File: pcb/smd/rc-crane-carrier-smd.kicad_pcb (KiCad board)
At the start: 2 copper layers, 90 x 64 mm, 32 parts, among them J1 BAT 2-3S, J10 SuperMini L, J11 SuperMini R, J12 DIAG0, J13 DIAG1, J2 Motor lift, J3 Motor tele, J4 RC lift, J5 RC tele, U2 TMC2209 #0 lift, U3 TMC2209 #1 tele, U4 AMS1117-5.0

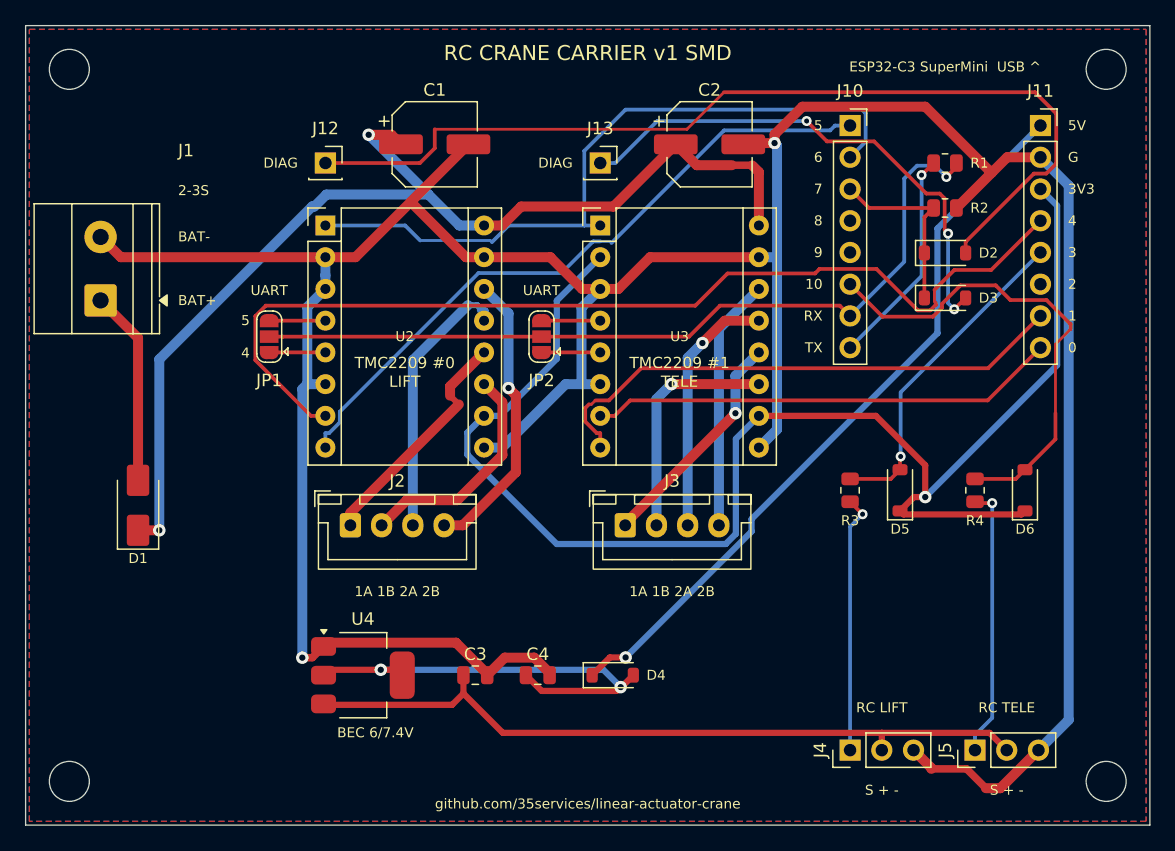
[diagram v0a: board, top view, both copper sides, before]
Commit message: PCB: power the drivers from the BEC, drop the battery input
The drivers' VM now comes from the ESC's BEC (6 V / 7.4 V, 4 A) through
the RC headers, like the ESP32's regulator. Removes the battery
terminal J1 and the reverse polarity diode D1 (the + pin in the middle
of the S + - header makes a reversed servo plug harmless), and the
board shrinks to 80 x 64 mm. Both variants: DRC 0 violations,
0 unconnected.

Co-Authored-By: Claude Opus 5.5 <noreply@anthropic.com>
Claude-Session: https://claude.ai/code/session_01JATcLE25KWRaki615r1Lis
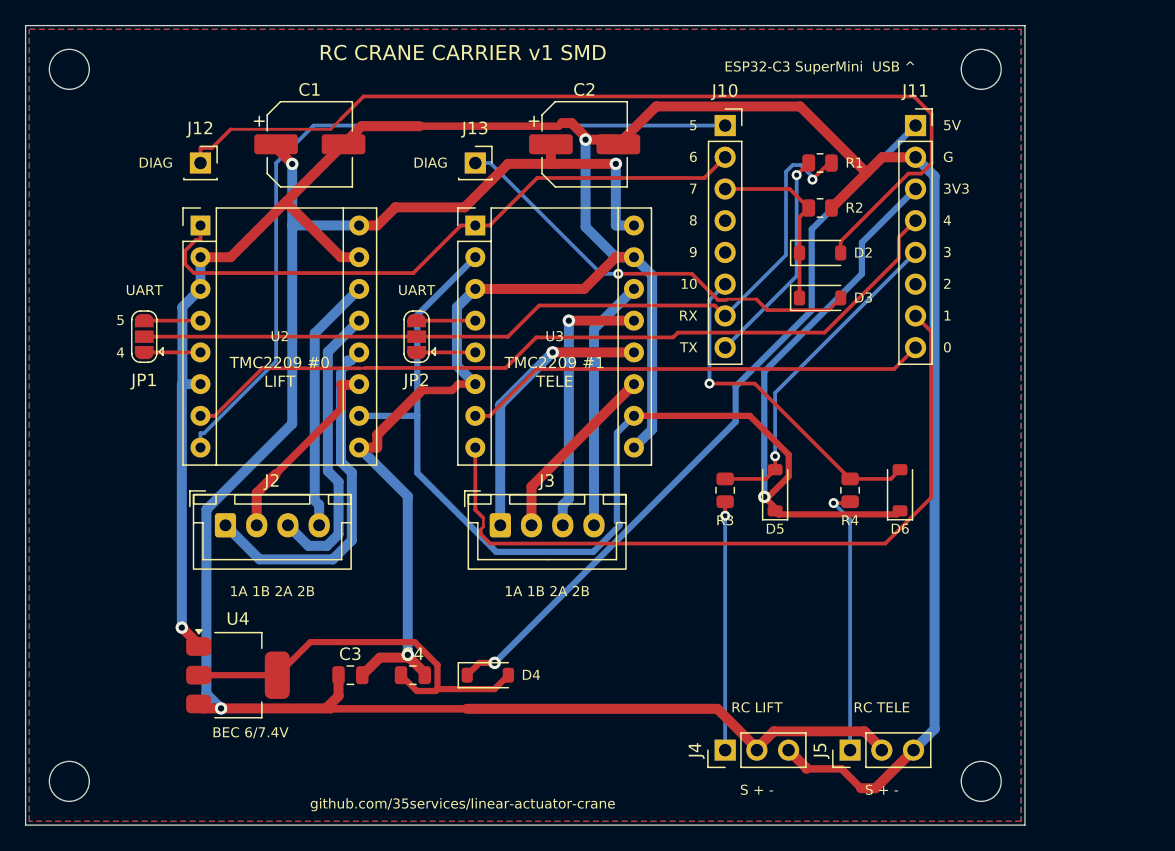
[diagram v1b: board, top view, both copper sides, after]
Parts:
- removed D1: SS34, Diode_SMD:D_SMA
- removed J1: BAT 2-3S, TerminalBlock_Phoenix:TerminalBlock_Phoenix_MKDS-1,5-2-5.08_1x02_P5.08mm_Horizontal
- moved C1 10.0 mm to (22.8, 9.50)
- moved C2 10.0 mm to (44.8, 9.50)
- moved C3 10.0 mm to (26.0, 52.0)
- moved C4 10.0 mm to (31.0, 52.0)
- moved D4 10.0 mm to (37.0, 52.0)
- moved D5 10.0 mm to (60.0, 37.2)
- moved D6 10.0 mm to (70.0, 37.2)
- moved H2 10.0 mm to (76.5, 3.50)
- moved H4 10.0 mm to (76.5, 60.5)
- moved J10 10.0 mm to (56.0, 8.00)
- moved J11 10.0 mm to (71.2, 8.00)
- moved J12 10.0 mm to (14.0, 11.0)
- moved J13 10.0 mm to (36.0, 11.0)
- moved J2 10.0 mm to (16.0, 40.0)
- moved J3 10.0 mm to (38.0, 40.0)
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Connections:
- C1 pad 1: VM -> VBEC
- C2 pad 1: VM -> VBEC
- U2 pad 16: VM -> VBEC
- U3 pad 16: VM -> VBEC
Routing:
- net VM: track 87.5 -> 0.00 mm, vias 2 -> 0
- net VBEC: track 59.8 -> 145.5 mm, vias 0 -> 3
- net DIR1: track 43.3 -> 60.2 mm
- net STEP0: track 80.6 -> 64.7 mm
- net VBAT_IN: track 15.6 -> 0.00 mm
- net RC1: track 38.7 -> 27.2 mm, vias 0 -> 1
- net M0_1A: track 18.9 -> 28.0 mm
- net DIR0: track 54.0 -> 62.6 mm
- net DIAG1: track 42.0 -> 34.6 mm, vias 3 -> 1
- net EN: track 57.1 -> 51.2 mm
- net M1_1B: track 18.8 -> 14.7 mm, vias 1 -> 0
- net M1_1A: track 18.3 -> 22.1 mm
- net +5V_REG: track 36.1 -> 32.6 mm, vias 2 -> 0
- net +3V3: track 115.8 -> 112.4 mm
- net M0_1B: track 18.3 -> 15.5 mm
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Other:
- board size 90 x 64 mm -> 80 x 64 mm
- board text removed: "2-3S"
- board text removed: "BAT+"
- board text removed: "BAT-"

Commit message: SMD board: 100 uF capacitors as THT, track JLCPCB extended parts
The SMD 100 uF electrolytic (C2836442) was the only extended part on the
SMD carrier. C1/C2 now use the THT footprint and are hand-soldered, so the
JLCPCB assembly has basic parts only. check_jlc_parts.py lists basic/extended
status and stock for every LCSC part in the BOMs.

Co-Authored-By: Claude Opus 5.5 <noreply@anthropic.com>
Claude-Session: https://claude.ai/code/session_01JATcLE25KWRaki615r1Lis
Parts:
- C1, C2: footprint Capacitor_SMD:CP_Elec_6.3x7.7 -> Capacitor_THT:CP_Radial_D8.0mm_P3.50mm
- moved C1 1.75 mm to (21.0, 9.50)
- moved C2 1.75 mm to (43.0, 9.50)
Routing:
- net DIAG0: track 76.8 -> 59.4 mm
- net GND: track 260.9 -> 250.5 mm, vias 3 -> 2
- net EN: track 51.2 -> 45.3 mm
- net DIR0: track 62.6 -> 65.9 mm
- net VBEC: track 145.5 -> 143.4 mm, vias 3 -> 1
- net +3V3: track 112.4 -> 111.7 mm
